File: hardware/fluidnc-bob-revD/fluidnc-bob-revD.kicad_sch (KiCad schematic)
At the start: 70 parts, among them J1 36V-IN, J10 RELAY, J11 AUX, J12 5V-EXT, J13 SD, J2 X-DRV, J3 Y-DRV, J4 Z-DRV, J5 LIM-X, J6 LIM-Y, J7 LIM-Z, J8 PROBE, J9 E-STOP, Q1 MMBT2222A, Q2 MMBT2222A, U1 SN74AHCT541N, U2 TSR 1-4850WI

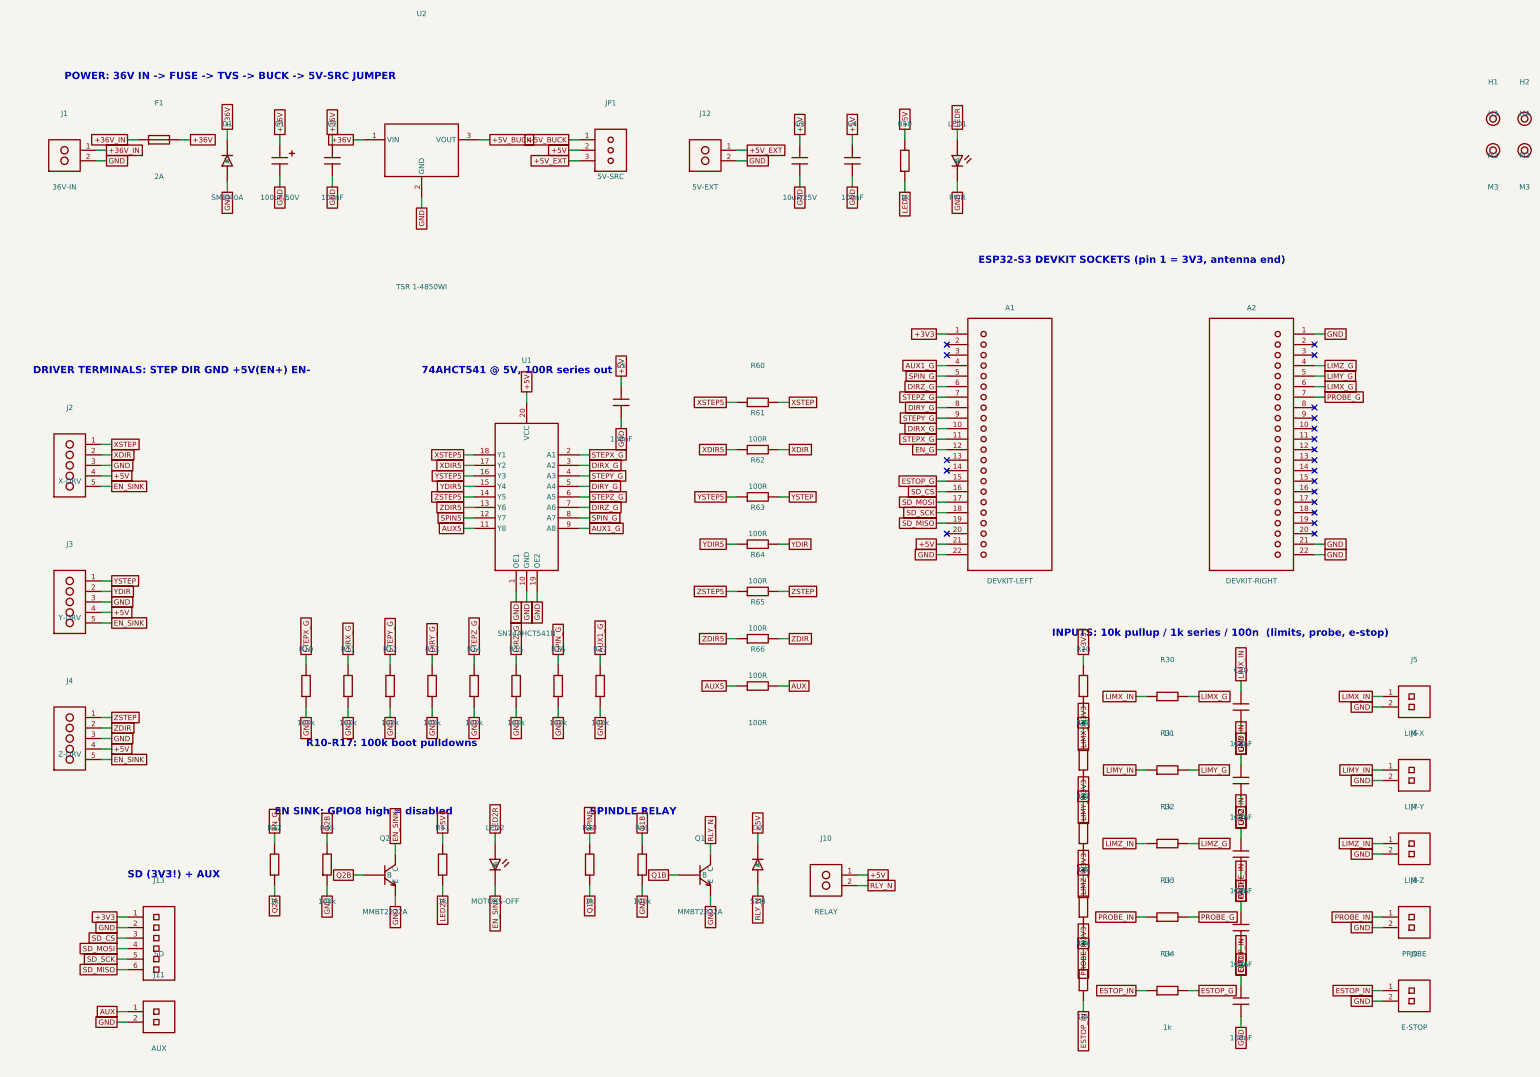
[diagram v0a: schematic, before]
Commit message: hardware: rev D schematic rework — drawn wires, rev C devkit parts, DK links
Per review: replace the label-everywhere schematic with a proper
drawn-wire one (rev C style): 172 wire segments, official power
symbols (+36V/+5V/+3V3/GND + PWR_FLAGs), 40 global labels left for
long-haul nets only. Single 44-pin devkit symbol + the proven rev C
ESP32_S3_DevKit_44_Socket footprint (copied to fluidnc-bob-revD.pretty).
Buffer channels reordered to devkit pad order (crossing-free bus;
GPIO map and config.yaml unchanged).

Every non-passive part now carries hidden Digikey and Datasheet URL
properties (verified product pages where available, search links
otherwise; R/C exempt). BOM/CSV: A1 socket = 2x PPTC221LFBN-RC on the
custom footprint; optional DigiKey spare devkit ESP32-S3-DEVKITC-1-N8.

verify_netlist.py switched to partition comparison (drawn nets get
KiCad auto-names) — it caught a real channel-order bug and two
diagonal-wire bugs before ERC did. ERC 0 violations; netlist verified.

Co-Authored-By: Claude Fable 5 <noreply@anthropic.com>
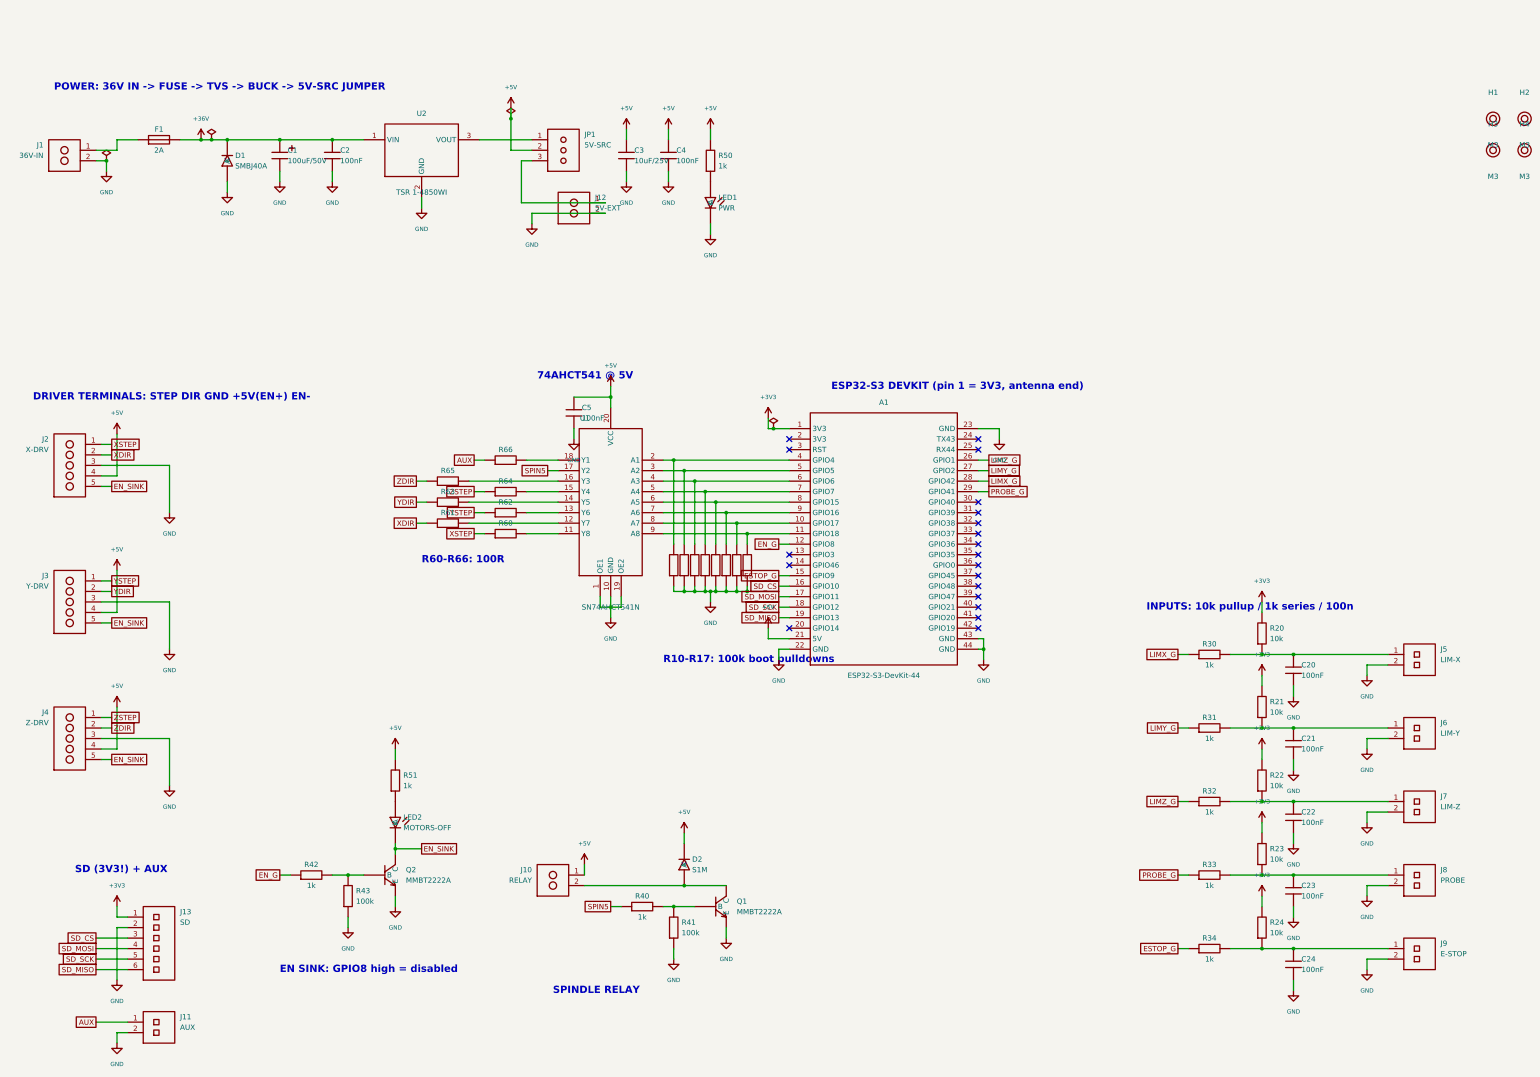
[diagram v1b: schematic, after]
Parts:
- removed A1: DEVKIT-LEFT, Connector_PinSocket_2.54mm:PinSocket_1x22_P2.54mm_Vertical, symbol bobD:CONN_1x22
- removed A2: DEVKIT-RIGHT, Connector_PinSocket_2.54mm:PinSocket_1x22_P2.54mm_Vertical, symbol bobD:CONN_1x22R
- removed R40, R42: 1k, Resistor_SMD:R_0805_2012Metric, symbol bobD:R
- added A1: ESP32-S3-DevKit-44, fluidnc-bob-revD:ESP32_S3_DevKit_44_Socket, symbol bobD:ESP32_S3_DevKit_44
- added R40, R42: 1k, Resistor_SMD:R_0805_2012Metric, symbol bobD:R_H
- D1: Digikey (none) -> https://www.digikey.com/en/products/result?keywords=SMBJ40A
- D2: Digikey (none) -> https://www.digikey.com/en/products/result?keywords=S1M-13-F
- F1: Digikey (none) -> https://www.digikey.com/en/products/detail/littelfuse-inc/0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
- J1, J10, J12: Digikey (none) -> https://www.digikey.com/en/products/detail/phoenix-contact/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
- J11, J5, J6, J7, J8, J9: Digikey (none) -> https://www.digikey.com/en/products/result?keywords=B2B-XH-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
- J13: Digikey (none) -> https://www.digikey.com/en/products/result?keywords=B6B-XH-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
- J2, J3, J4: Digikey (none) -> https://www.digikey.com/en/products/result?keywords=1715750
- JP1: Digikey (none) -> https://www.digikey.com/en/products/result?keywords=PRPC040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
- LED1: Digikey (none) -> https://www.digikey.com/en/products/result?keywords=WP7113GD
- LED2: Digikey (none) -> https://www.digikey.com/en/products/result?keywords=WP7113ID
- Q1, Q2: Digikey (none) -> https://www.digikey.com/en/products/result?keywords=MMBT222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
- U1: Digikey (none) -> https://www.digikey.com/en/products/detail/texas-instrument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
- U2: Digikey (none) -> https://www.digikey.com/en/products/detail/traco-power/TSR-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
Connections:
- net +3V3: now also A1.1 (3V3)
- net +5V: now also A1.21 (5V)
- net AUX: now also R66.1; no longer R66.2
- net EN_G: now also A1.12 (GPIO8), R42.1
- net ESTOP_G: now also R34.1, A1.15 (GPIO9); no longer R34.2
- net GND: now also A1.22 (GND), A1.23 (GND), A1.43 (GND), A1.44 (GND)
- net LIMX_G: now also R30.1, A1.28 (GPIO42); no longer R30.2
- net LIMY_G: now also R31.1, A1.27 (GPIO2); no longer R31.2
- net LIMZ_G: now also R32.1, A1.26 (GPIO1); no longer R32.2
- net PROBE_G: now also R33.1, A1.29 (GPIO41); no longer R33.2
- net SD_CS: now also A1.16 (GPIO10)
- net SD_MISO: now also A1.19 (GPIO13)
- net SD_MOSI: now also A1.17 (GPIO11)
- net SD_SCK: now also A1.18 (GPIO12)
- net SPIN5: now also U1.17 (Y2), R40.1; no longer U1.12 (Y7)
- net XDIR: now also R61.1; no longer R61.2
- net XSTEP: now also R60.1; no longer R60.2
- net YDIR: now also R63.1; no longer R63.2
- net YSTEP: now also R62.1; no longer R62.2
- net ZDIR: now also R65.1; no longer R65.2
- net ZSTEP: now also R64.1; no longer R64.2
- net +36V_IN: no longer names the net of F1.1, J1.1
- net +5V_BUCK: no longer names the net of JP1.1, U2.3 (VOUT)
- net +5V_EXT: no longer names the net of J12.1, JP1.3
- net AUX1_G: no longer names the net of R17.1, U1.9 (A8)
- net AUX1_G: now also A1.11 (GPIO18)
- net AUX5: no longer names the net of U1.11 (Y8)
- net AUX5: now also R60.2; no longer R66.1
- net DIRX_G: no longer names the net of R11.1, U1.3 (A2)
- net DIRX_G: now also A1.5 (GPIO5)
- net DIRY_G: no longer names the net of R13.1, U1.5 (A4)
- net DIRY_G: now also A1.7 (GPIO7)
- net DIRZ_G: no longer names the net of R15.1, U1.7 (A6)
- net DIRZ_G: now also A1.9 (GPIO16)
- net ESTOP_IN: no longer names the net of C24.1, J9.1, R24.2
- net ESTOP_IN: now also R34.2; no longer R34.1
- net LED2R: no longer names the net of LED2.2 (A), R51.2
- net LEDR: no longer names the net of LED1.2 (A), R50.2
- net LIMX_IN: no longer names the net of C20.1, J5.1, R20.2
- net LIMX_IN: now also R30.2; no longer R30.1
- net LIMY_IN: no longer names the net of C21.1, J6.1, R21.2
- net LIMY_IN: now also R31.2; no longer R31.1
- net LIMZ_IN: no longer names the net of C22.1, J7.1, R22.2
- net LIMZ_IN: now also R32.2; no longer R32.1
- net PROBE_IN: no longer names the net of C23.1, J8.1, R23.2
- net PROBE_IN: now also R33.2; no longer R33.1
- net Q1B: no longer names the net of Q1.1 (B), R41.1
- net Q1B: now also R40.2
- net Q2B: no longer names the net of Q2.1 (B), R43.1
- net Q2B: now also R42.2
- net RLY_N: no longer names the net of D2.2 (A), J10.2, Q1.3 (C)
- net SPIN_G: no longer names the net of R16.1, U1.8 (A7)
- net SPIN_G: now also A1.10 (GPIO17)
- net STEPX_G: no longer names the net of R10.1, U1.2 (A1)
- net STEPX_G: now also A1.4 (GPIO4)
- net STEPY_G: no longer names the net of R12.1, U1.4 (A3)
- net STEPY_G: now also A1.6 (GPIO6)
- net STEPZ_G: no longer names the net of R14.1, U1.6 (A5)
- net STEPZ_G: now also A1.8 (GPIO15)
- removed net XDIR5: R61.1, U1.17 (Y2)
- net XSTEP5: no longer names the net of U1.18 (Y1)
- net XSTEP5: now also R66.2; no longer R60.1
- net YDIR5: no longer names the net of U1.15 (Y4)
- net YDIR5: now also R64.2; no longer R63.1
- net YSTEP5: no longer names the net of U1.16 (Y3)
- net YSTEP5: now also R65.2; no longer R62.1
- net ZDIR5: no longer names the net of U1.13 (Y6)
- net ZDIR5: now also R62.2; no longer R65.1
- net ZSTEP5: no longer names the net of U1.14 (Y5)
- net ZSTEP5: now also R63.2; no longer R64.1
- new net: R61.2, U1.12 (Y7)
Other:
- note added: "74AHCT541 @ 5V"
- note added: "ESP32-S3 DEVKIT (pin 1 = 3V3, antenna end)"
- note added: "INPUTS: 10k pullup / 1k series / 100n"
- note added: "R60-R66: 100R"
- note removed: "74AHCT541 @ 5V, 100R series out"
- note removed: "ESP32-S3 DEVKIT SOCKETS (pin 1 = 3V3, antenna end)"
- note removed: "INPUTS: 10k pullup / 1k series / 100n (limits, probe, e-stop)"
